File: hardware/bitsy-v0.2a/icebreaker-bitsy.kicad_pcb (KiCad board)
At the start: 4 copper layers, 38.1 x 17.8 mm, 99 parts, among them J1 Conn_01x01, J10 Conn_01x01, J11 Conn_01x01, J12 Conn_01x01, J13 Conn_01x01, J14 Jumper, J15 Jumper, J16 Jumper, J17 Jumper, J18 Jumper, J19 Jumper, J2 Conn_01x01, J20 Conn_01x01, J21 Conn_01x01, J22 Conn_01x01, J23 Conn_01x01, J24 Conn_01x01, J25 Conn_01x01, J26 Conn_01x01, J27 Conn_01x01, J28 Conn_01x01, J29 Conn_01x01, J3 Conn_01x01, J30 Conn_01x01, J31 Conn_01x01, J32 Conn_01x01, J33 Conn_01x01, J34 Conn_01x01, J35 Conn_01x01, J36 Conn_01x01, J37 Conn_01x01, J38 Jumper, J4 Conn_01x01, J41 Conn_01x01, J42 Conn_01x01, J43 Conn_01x01, J44 Conn_01x01, J45 Conn_01x01, J46 Conn_01x01, J47 Conn_01x01, J48 Conn_01x01, J49 Conn_01x01, J5 Conn_01x01, J6 Conn_01x01, J7 Conn_01x01, J8 Conn_01x01, J9 Conn_01x01, P1 USB_OTG, P2 UP, P3 UP, P4 UP, P5 UP, SW1 TACT, U1 USBLC6-2, U2 3.3V, U3 1V2, U5 W25Q, U6 ICE5LP4K-SG48, X1 12MHz

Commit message: Fixed pin header 3d models.
We had some of the models doubled up or not fully disabled. Now the TH
pin headers are all using KiCad V5 3d model locations and are all
disabled.

This fixes #23
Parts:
- removed REF**: 1b2_Logo_SilkS_5mm, pkl_logos:1b2_Logo_SilkS_5mm
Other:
- board text removed: "1Bitsquared (C) 2018"

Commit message: Added more legend silkscreen to ears.
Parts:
- added REF**: 1b2_Logo_SilkS_5mm, pkl_logos:1b2_Logo_SilkS_5mm, B.Cu at (41.6, 47.4)
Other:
- board text added: "1Bitsquared (C) 2018"
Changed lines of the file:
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@@
   (general
     (thickness 1.6)
-    (drawings 160)
+    (drawings 161)
     (tracks 696)
     (zones 0)
-    (modules 98)
+    (modules 99)
     (nets 61)
   )
@@
     (add_net "Net-(R7-Pad2)")
     (add_net "Net-(X1-Pad2)")
+  )
+  (module pkl_logos:1b2_Logo_SilkS_5mm locked (layer B.Cu)
+    (at 41.628314 47.429988 90)
+    (fp_text reference REF** (at 0 -4 90) (layer B.Fab) hide
+      (effects (font (size 1 1) (thickness 0.15)) (justify mirror))
+    )
+    (fp_text value 1b2_Logo_SilkS_5mm (at 0 4 90) (layer B.Fab) hide
+      (effects (font (size 1 1) (thickness 0.15)) (justify mirror))
+    )
+    (fp_line (start -0.5 0.5) (end -0.5 2.5) (layer B.SilkS) (width 0.2))
+    (fp_line (start -0.5 2.5) (end -2.5 2.5) (layer B.SilkS) (width 0.2))
+    (fp_line (start -2.5 2.5) (end -2.5 0.5) (layer B.SilkS) (width 0.2))
+    (fp_line (start -2.5 0.5) (end -0.5 0.5) (layer B.SilkS) (width 0.2))
+    (fp_line (start -0.5 2.5) (end 0 2) (layer B.SilkS) (width 0.2))
+    (fp_line (start 0 2) (end 0 0) (layer B.SilkS) (width 0.2))
+    (fp_line (start 0 0) (end -0.5 0.5) (layer B.SilkS) (width 0.2))
+    (fp_line (start -2.5 0.5) (end -2 0) (layer B.SilkS) (width 0.2))
+    (fp_line (start -2 0) (end 0 0) (layer B.SilkS) (width 0.2))
+    (fp_line (start 2 2) (end 0.5 2) (layer B.SilkS) (width 0.2))
+    (fp_line (start 0.5 2) (end 0.5 -0.5) (layer B.SilkS) (width 0.2))
+    (fp_line (start 0.5 -0.5) (end -2 -0.5) (layer B.SilkS) (width 0.2))
+    (fp_line (start -2 -0.5) (end -2 -2) (layer B.SilkS) (width 0.2))
+    (fp_line (start -2 -2) (end 2 -2) (layer B.SilkS) (width 0.2))
+    (fp_line (start 2 -2) (end 2 2) (layer B.SilkS) (width 0.2))
+    (fp_line (start 2 2) (end 2.5 1.5) (layer B.SilkS) (width 0.2))
+    (fp_line (start 2.5 1.5) (end 2.5 -2.5) (layer B.SilkS) (width 0.2))
+    (fp_line (start 2.5 -2.5) (end 2 -2) (layer B.SilkS) (width 0.2))
+    (fp_line (start -2 -2) (end -1.5 -2.5) (layer B.SilkS) (width 0.2))
+    (fp_line (start -1.5 -2.5) (end 2.5 -2.5) (layer B.SilkS) (width 0.2))
   )
   (module pkl_housings_dfn_qfn:QFN-48-1EP_7x7mm_Pitch0.5mm (layer F.Cu)
@@
       (net 2 +3V3))
   )
+  (gr_text "1Bitsquared\n(C) 2018" (at 37.4 47.3 270) (layer B.SilkS)
+    (effects (font (size 1 1) (thickness 0.25)) (justify mirror))
+  )
   (gr_line (start 79.2 38.6) (end 79.2 47.5) (layer Cmts.User) (width 0.2))

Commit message: Replaced/added the null logo to the boards.
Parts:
- REF**: value 1b2_Logo_SilkS_5mm -> null_Logo_SilkS_5mm; footprint pkl_logos:1b2_Logo_SilkS_5mm -> pkl_logos:null_Logo_SilkS_5mm
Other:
- board text added: "NULL"
- board text removed: "1Bitsquared (C) 2018"
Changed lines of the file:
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@@
-(kicad_pcb (version 20171130) (host pcbnew 5.1.2-f72e74a~84~ubuntu18.04.1)
+(kicad_pcb (version 20171130) (host pcbnew 5.1.5-52549c5~86~ubuntu19.10.1)
   (general
     (thickness 1.6)
@@
     (add_net "Net-(X1-Pad2)")
   )
-  (module pkl_logos:1b2_Logo_SilkS_5mm locked (layer B.Cu)
+  (module pkl_logos:null_Logo_SilkS_5mm locked (layer B.Cu)
     (at 41.628314 47.429988 90)
     (fp_text reference REF** (at 0 -4 90) (layer B.Fab) hide
       (effects (font (size 1 1) (thickness 0.15)) (justify mirror))
     )
-    (fp_text value 1b2_Logo_SilkS_5mm (at 0 4 90) (layer B.Fab) hide
+    (fp_text value null_Logo_SilkS_5mm (at 0 4 90) (layer B.Fab) hide
       (effects (font (size 1 1) (thickness 0.15)) (justify mirror))
     )
-    (fp_line (start -0.5 0.5) (end -0.5 2.5) (layer B.SilkS) (width 0.2))
-    (fp_line (start -0.5 2.5) (end -2.5 2.5) (layer B.SilkS) (width 0.2))
-    (fp_line (start -2.5 2.5) (end -2.5 0.5) (layer B.SilkS) (width 0.2))
-    (fp_line (start -2.5 0.5) (end -0.5 0.5) (layer B.SilkS) (width 0.2))
-    (fp_line (start -0.5 2.5) (end 0 2) (layer B.SilkS) (width 0.2))
-    (fp_line (start 0 2) (end 0 0) (layer B.SilkS) (width 0.2))
-    (fp_line (start 0 0) (end -0.5 0.5) (layer B.SilkS) (width 0.2))
-    (fp_line (start -2.5 0.5) (end -2 0) (layer B.SilkS) (width 0.2))
-    (fp_line (start -2 0) (end 0 0) (layer B.SilkS) (width 0.2))
-    (fp_line (start 2 2) (end 0.5 2) (layer B.SilkS) (width 0.2))
-    (fp_line (start 0.5 2) (end 0.5 -0.5) (layer B.SilkS) (width 0.2))
-    (fp_line (start 0.5 -0.5) (end -2 -0.5) (layer B.SilkS) (width 0.2))
-    (fp_line (start -2 -0.5) (end -2 -2) (layer B.SilkS) (width 0.2))
-    (fp_line (start -2 -2) (end 2 -2) (layer B.SilkS) (width 0.2))
-    (fp_line (start 2 -2) (end 2 2) (layer B.SilkS) (width 0.2))
-    (fp_line (start 2 2) (end 2.5 1.5) (layer B.SilkS) (width 0.2))
-    (fp_line (start 2.5 1.5) (end 2.5 -2.5) (layer B.SilkS) (width 0.2))
-    (fp_line (start 2.5 -2.5) (end 2 -2) (layer B.SilkS) (width 0.2))
-    (fp_line (start -2 -2) (end -1.5 -2.5) (layer B.SilkS) (width 0.2))
-    (fp_line (start -1.5 -2.5) (end 2.5 -2.5) (layer B.SilkS) (width 0.2))
+    (fp_arc (start -0.4 -0.2) (end -0.7 -0.2) (angle 180) (layer B.SilkS) (width 0.15))
+    (fp_line (start 1 -0.5) (end 1.5 -0.5) (layer B.SilkS) (width 0.15))
+    (fp_line (start 1 0.5) (end 1 -0.5) (layer B.SilkS) (width 0.15))
+    (fp_line (start 0.2 -0.5) (end 0.7 -0.5) (layer B.SilkS) (width 0.15))
+    (fp_line (start 0.2 0.5) (end 0.2 -0.5) (layer B.SilkS) (width 0.15))
+    (fp_line (start -0.1 0.5) (end -0.1 -0.2) (layer B.SilkS) (width 0.15))
+    (fp_line (start -0.7 0.5) (end -0.7 -0.2) (layer B.SilkS) (width 0.15))
+    (fp_line (start -1 -0.5) (end -1 0.5) (layer B.SilkS) (width 0.15))
+    (fp_line (start -1.5 0.5) (end -1 -0.5) (layer B.SilkS) (width 0.15))
+    (fp_line (start -1.5 -0.5) (end -1.5 0.5) (layer B.SilkS) (width 0.15))
+    (fp_line (start 2.5 2.5) (end -2.5 2.5) (layer B.SilkS) (width 0.2))
+    (fp_line (start -2.5 2.5) (end -2.5 -2.5) (layer B.SilkS) (width 0.2))
+    (fp_line (start 2.5 2.5) (end 2.5 -2.5) (layer B.SilkS) (width 0.2))
+    (fp_line (start -2.5 -2.5) (end 2.5 -2.5) (layer B.SilkS) (width 0.2))
   )
   (module pkl_housings_dfn_qfn:QFN-48-1EP_7x7mm_Pitch0.5mm (layer F.Cu)
@@
       (net 2 +3V3))
   )
-  (gr_text "1Bitsquared\n(C) 2018" (at 37.4 47.3 270) (layer B.SilkS)
+  (gr_text NULL (at 37.4 47.3 270) (layer B.SilkS)
     (effects (font (size 1 1) (thickness 0.25)) (justify mirror))
   )

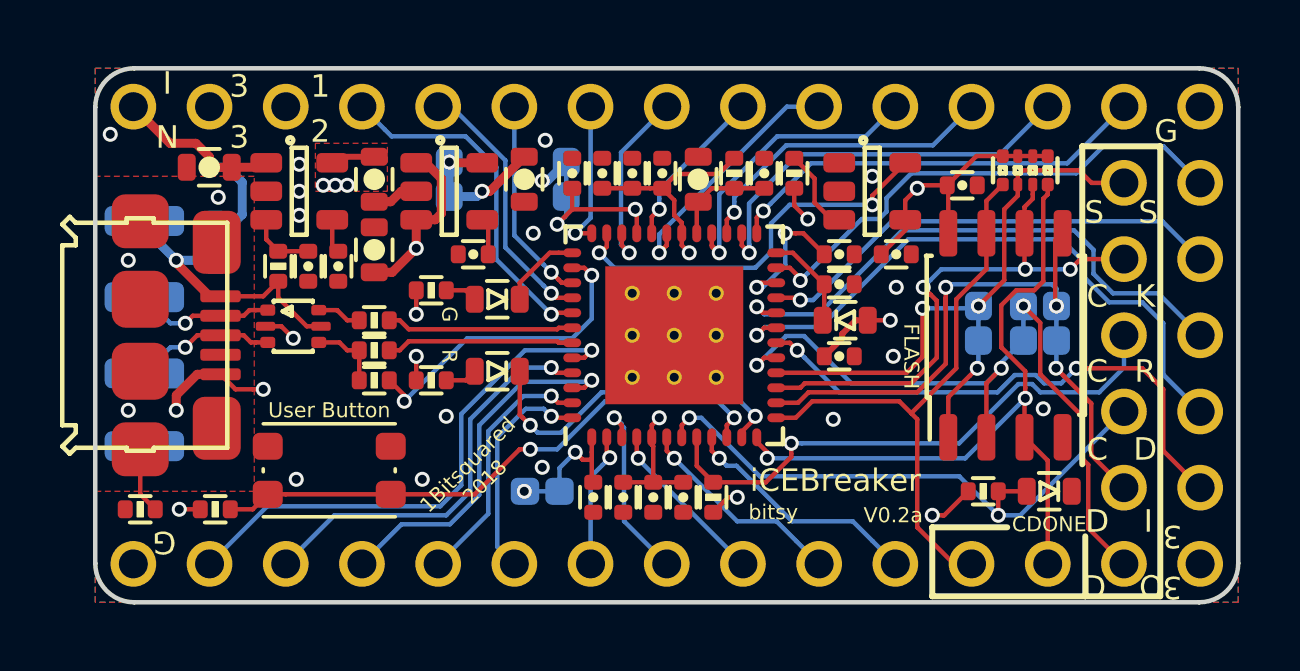
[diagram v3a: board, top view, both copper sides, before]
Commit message: Updated all design files to KiCad V8.0.6.
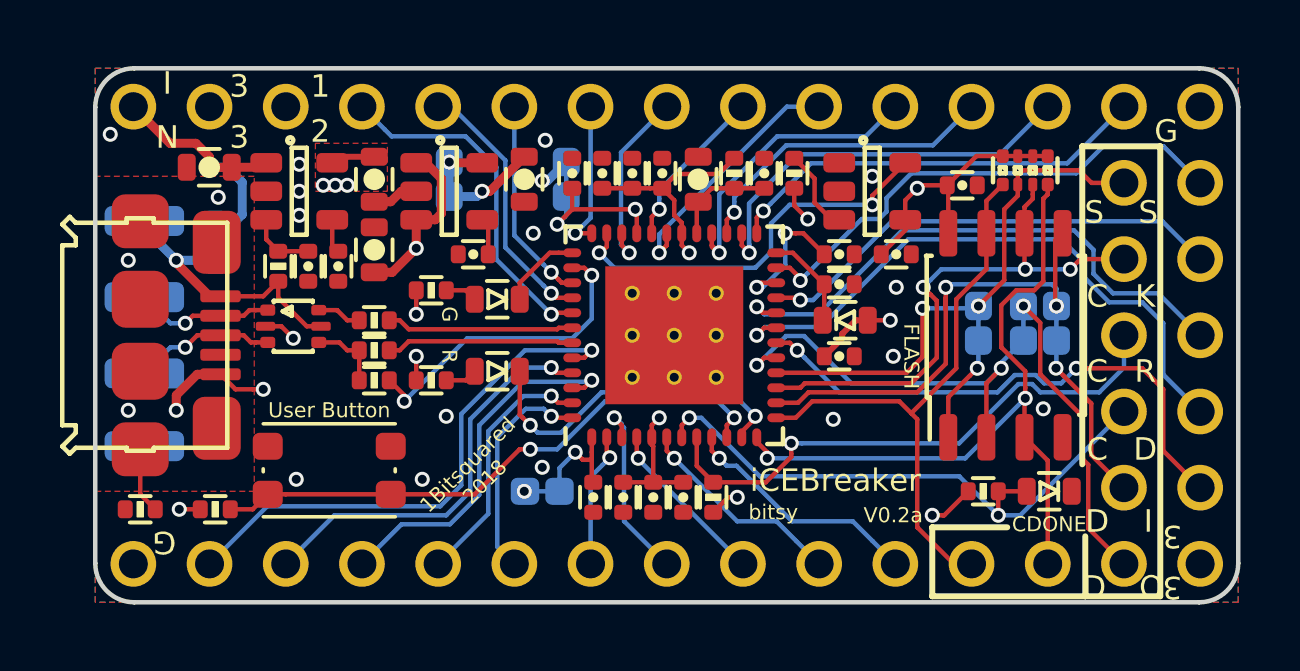
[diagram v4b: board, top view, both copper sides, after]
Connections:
- net /FLASH_~HLD~/~RST~/IO3 renamed /FLASH_~{HLD}/~{RST}/IO3
- net /FLASH_~WP~/IO2 renamed /FLASH_~{WP}/IO2
- net /~BUTTON renamed /~{BUTTON}
- net /~LEDG renamed /~{LEDG}
- net /~LEDR renamed /~{LEDR}
- net /~LED_BLU renamed /~{LED_BLU}
- net /~LED_GRN renamed /~{LED_GRN}
- net /~LED_RED renamed /~{LED_RED}
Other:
- net class Default removed
- board text added: "25 39 ~{LED_RED}"
- board text added: "26 40 ~{LED_GRN}"
- board text added: "27 41 ~{LED_BLU}"
- board text added: "IOB_22A FLASH_~{WP}/IO2 12 13"
- board text added: "IOB_24A FLASH_~{HLD}/~{RST}/IO3 13 12"
- board text removed: "25 39 ~LED_RED"
- board text removed: "26 40 ~LED_GRN"
- board text removed: "27 41 ~LED_BLU"
- board text removed: "IOB_22A FLASH_~WP~/IO2 12 13"
- board text removed: "IOB_24A FLASH_~HLD~/~RST~/IO3 13 12"
